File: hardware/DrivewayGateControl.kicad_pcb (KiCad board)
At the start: 2 copper layers, 99.7 x 99.1 mm, 51 parts, among them J3 power, K1 relay1, K2 relay2, K3 relay3, K4 relay4, Q1 2N3906, Q2 2N3906, Q3 2N3906, Q4 2N3906, SW1 SW_Push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

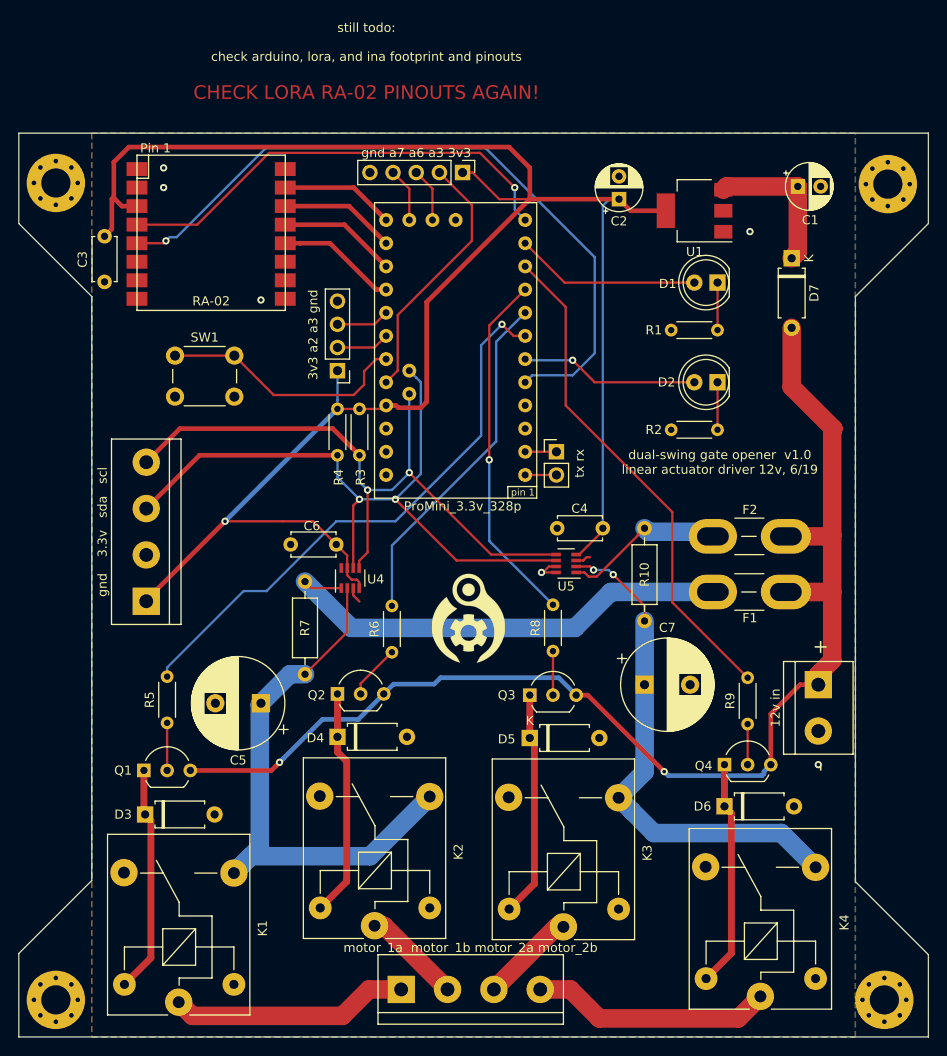
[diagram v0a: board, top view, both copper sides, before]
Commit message: update silkscreen, add more pin breakouts
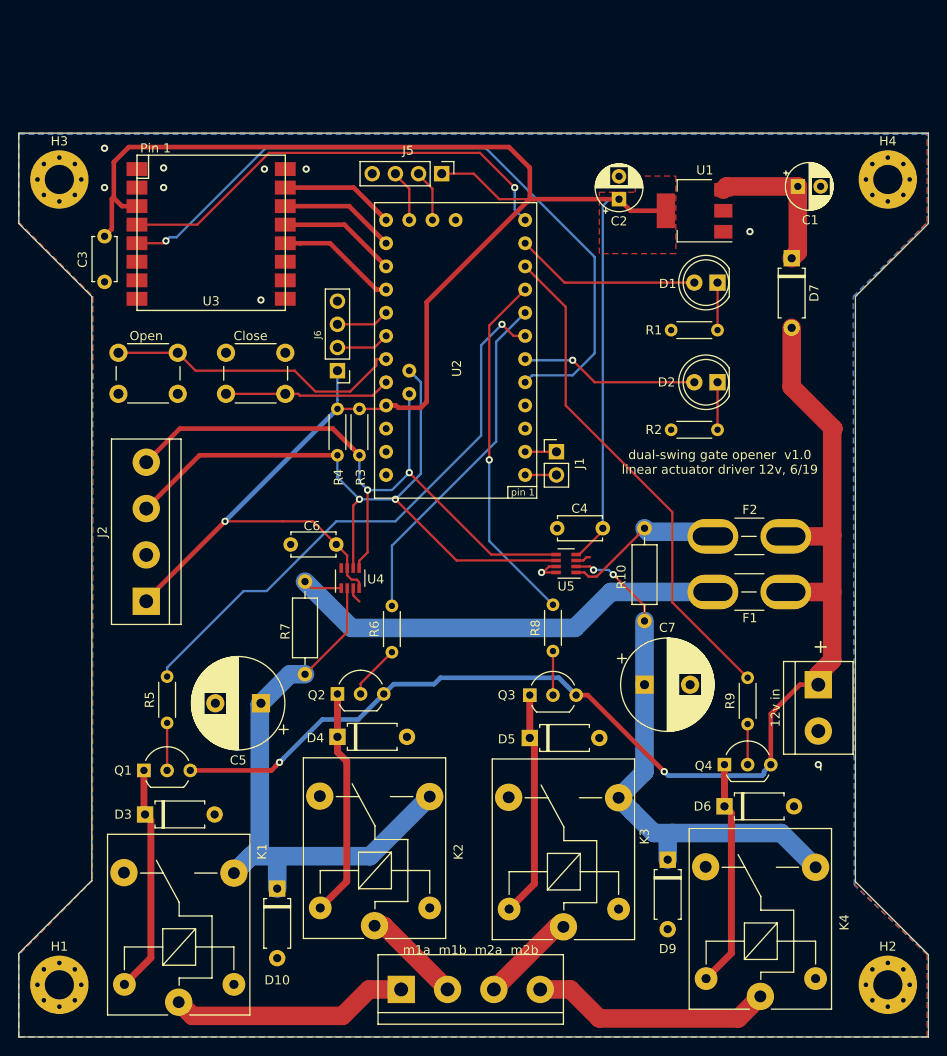
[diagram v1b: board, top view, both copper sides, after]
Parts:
- removed G***: LOGO_MWM, MainWorking:LOGO_MWM
- removed gnd a7 a6 a3 3v3: gpio1, Connector_PinHeader_2.54mm:PinHeader_1x05_P2.54mm_Vertical
- added D10: D, Diode_THT:D_A-405_P7.62mm_Horizontal, F.Cu at (91.8, 120.3)
- added D9: 1n4001, Diode_THT:D_A-405_P7.62mm_Horizontal, F.Cu at (134.6, 117.1)
- added J5: gpio1, Connector_PinHeader_2.54mm:PinHeader_1x04_P2.54mm_Vertical, F.Cu at (109.9, 41.9)
- added SW2: open, Button_Switch_THT:SW_PUSH_6mm_H8.5mm, F.Cu at (92.7, 66.0)
- D3, D4, D5, D6: value D -> 1n4001
- H1, H2, H3, H4: value MountingHole -> MountingHole_Pad
- J1: renamed from tx rx
- J2: renamed from gnd    3.3v   sda   scl; value Conn_01x04 -> magnetometer
- J4: renamed from motor_1a  motor_1b motor_2a motor_2b
- J6: renamed from 3v3 a2 a3 gnd
- R10, R7: value 100 -> 0.1
- SW1: value SW_Push -> close
- moved H3 89.9 mm to (67.9, 42.5)
- moved H1 87.9 mm to (67.9, 130.8)
- moved SW1 6.21 mm to (74.4, 61.5)
- moved H2 1.69 mm to (158.8, 130.8)
- moved H4 0.51 mm to (158.8, 42.5)
- renumbered ProMini_3.3v_328p to U2, RA-02 to U3
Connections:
- H1 pad 1: (no net) -> GND
- H2 pad 1: (no net) -> GND
- H3 pad 1: (no net) -> GND
- H4 pad 1: (no net) -> GND
- U2 pad A3: /a3 -> /sw2
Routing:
- net /a3: track 28.4 -> 0.00 mm
- net /sw2: track 0.00 -> 18.2 mm
- net /sw1: track 27.4 -> 33.0 mm
- net Net-(1n4001-Pad1): track 62.3 -> 66.1 mm
- net Net-(C7-Pad1): track 56.2 -> 59.4 mm
- net +3V3: track 218.9 -> 221.1 mm
- net GND: vias 6 -> 10
- added copper zone on F.Cu, net +3V3
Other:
- board text added: "Close"
- board text added: "Open"
- board text added: "m1a m1b m2a m2b"
- board text removed: "CHECK LORA RA-02 PINOUTS AGAIN!"
- board text removed: "check arduino, lora, and ina footprint and pinouts"
- board text removed: "still todo:"

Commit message: fixed relay switch issue
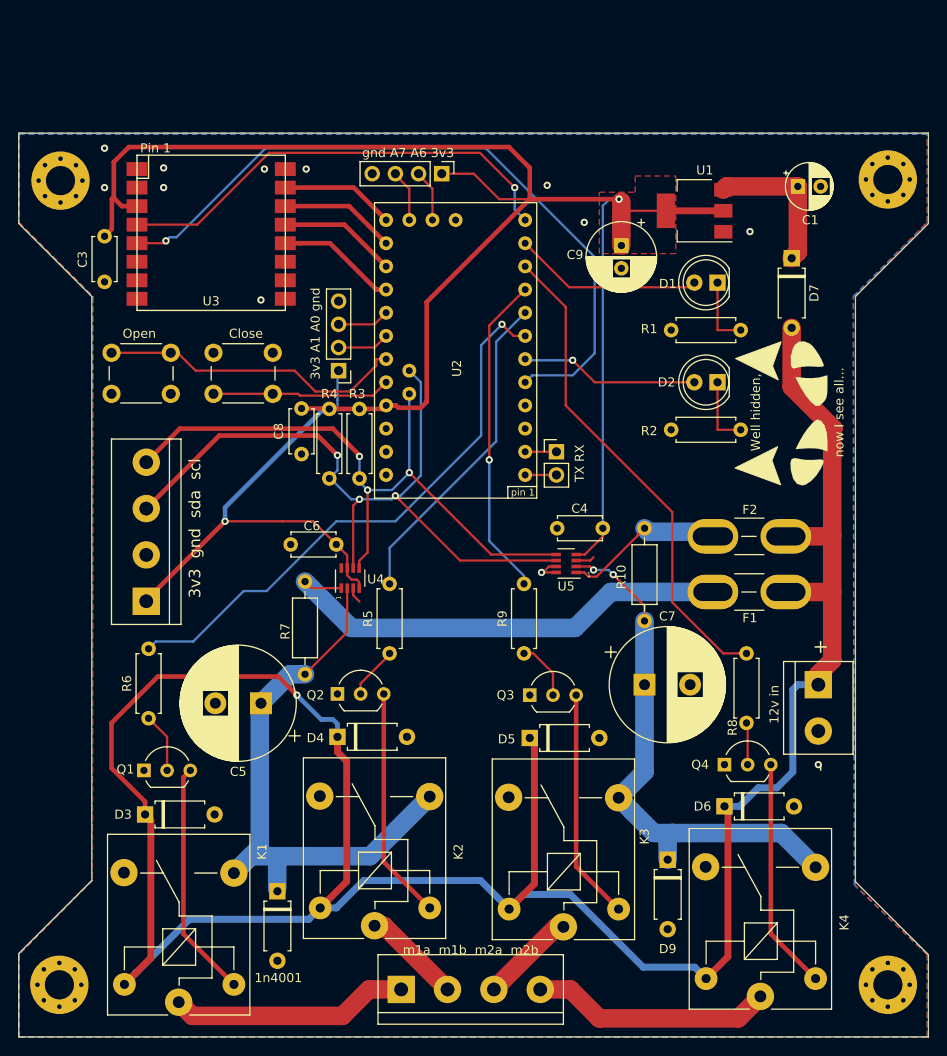
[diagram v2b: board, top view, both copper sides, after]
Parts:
- removed C2: 22uf, Capacitor_THT:CP_Radial_D5.0mm_P2.50mm
- removed D10: D, Diode_THT:D_A-405_P7.62mm_Horizontal
- added 1n4001: D, Diode_THT:D_A-405_P7.62mm_Horizontal, F.Cu at (91.8, 120.6)
- added C8: 0.1uf, Capacitor_THT:C_Disc_D4.7mm_W2.5mm_P5.00mm, F.Cu at (94.5, 72.6)
- added C9: 100uf, Capacitor_THT:CP_Radial_D7.5mm_P2.50mm, F.Cu at (129.5, 49.8)
- added G***: LOGO, MainWorking:cateyes_small_ears, F.Cu at (150.4, 68.1)
- added G***: LOGO_MWM_med, MainWorking:LOGO_MWM_med, B.Cu at (111.3, 54.9)
- C1: value 10uf -> 22uf
- C3, C4, C6: value C -> 0.1uf
- C5, C7: value CP -> 470uf; footprint Capacitor_THT:CP_Radial_D10.0mm_P5.00mm -> Capacitor_THT:CP_Radial_D12.5mm_P5.00mm
- Q1, Q2, Q3, Q4: value 2N3906 -> 2N3904
- R1, R2, R3, R4, R5, R6, R8, R9: footprint Resistor_THT:R_Axial_DIN0204_L3.6mm_D1.6mm_P5.08mm_Horizontal -> Resistor_THT:R_Axial_DIN0207_L6.3mm_D2.5mm_P7.62mm_Horizontal
- moved R6 27.6 mm to (77.7, 101.6)
- moved R9 25.7 mm to (118.9, 94.5)
- moved R5 25.5 mm to (104.1, 94.5)
- moved R8 22.6 mm to (143.3, 102.1)
- moved SW2 1.37 mm to (91.3, 66.0)
- moved R4 0.89 mm to (97.5, 67.7)
- moved SW1 0.76 mm to (73.7, 61.5)
- moved H3 0.18 mm to (68.1, 42.7), turned to 270 degrees
- moved J6 0.13 mm to (98.6, 63.5)
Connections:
- D3 pad 1: Net-(D3-Pad1) -> +12V
- D4 pad 1: Net-(D4-Pad1) -> +12V
- D5 pad 1: Net-(D5-Pad1) -> +12V
- D6 pad 1: Net-(D6-Pad1) -> +12V
- K1 pad 2: GND -> Net-(K1-Pad2)
- K1 pad 5: Net-(D3-Pad1) -> +12V
- K2 pad 2: GND -> Net-(K2-Pad2)
- K2 pad 5: Net-(D4-Pad1) -> +12V
- K3 pad 2: GND -> Net-(K3-Pad2)
- K3 pad 5: Net-(D5-Pad1) -> +12V
- K4 pad 2: GND -> Net-(K4-Pad2)
- K4 pad 5: Net-(D6-Pad1) -> +12V
- Q1 pad 1: Net-(D3-Pad1) -> GND
- Q1 pad 3: +12V -> Net-(K1-Pad2)
- Q2 pad 1: Net-(D4-Pad1) -> GND
- Q2 pad 3: +12V -> Net-(K2-Pad2)
- Q3 pad 1: Net-(D5-Pad1) -> GND
- Q3 pad 3: +12V -> Net-(K3-Pad2)
- Q4 pad 1: Net-(D6-Pad1) -> GND
- Q4 pad 3: +12V -> Net-(K4-Pad2)
- R5 pad 1: Net-(Q1-Pad2) -> Net-(Q2-Pad2)
- R5 pad 2: /relay1 -> /relay2
- R6 pad 1: Net-(Q2-Pad2) -> Net-(Q1-Pad2)
- R6 pad 2: /relay2 -> /relay1
- R8 pad 1: Net-(Q3-Pad2) -> Net-(Q4-Pad2)
- R8 pad 2: /relay3 -> /relay4
- R9 pad 1: Net-(Q4-Pad2) -> Net-(Q3-Pad2)
- R9 pad 2: /relay4 -> /relay3
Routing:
- net +12V: track 136.9 -> 270.0 mm, vias 2 -> 1
- net +3V3: track 221.1 -> 249.9 mm, vias 1 -> 2
- net Net-(K1-Pad2): track 0.00 -> 26.1 mm
- net Net-(K2-Pad2): track 0.00 -> 25.5 mm
- net Net-(K4-Pad2): track 0.00 -> 25.5 mm
- net Net-(K3-Pad2): track 0.00 -> 25.4 mm
- net Net-(D4-Pad1): track 25.1 -> 0.00 mm
- net Net-(D3-Pad1): track 25.0 -> 0.00 mm
- net Net-(D6-Pad1): track 24.9 -> 0.00 mm
- net Net-(D5-Pad1): track 24.8 -> 0.00 mm
- net /relay3: track 39.1 -> 35.5 mm
- net /sda: track 77.1 -> 80.5 mm, vias 2 -> 3
- net Net-(D2-Pad1): track 5.21 -> 7.75 mm
- net Net-(D1-Pad1): track 5.21 -> 7.75 mm
- net /relay2: track 38.2 -> 35.9 mm
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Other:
- board text added: "1"
- board text added: "3v3 A1 A0 gnd"
- board text added: "3v3 gnd sda scl"
- board text added: "LoRa H-Bridge gate ctrl w/ magnetic alarm rev 1.1 8/19"
- board text added: "TX RX"
- board text added: "Well hidden,"
- board text added: "gnd A7 A6 3v3"
- board text added: "now I see all..."
- board text removed: "dual-swing gate opener v1.0 linear actuator driver 12v, 6/19"
